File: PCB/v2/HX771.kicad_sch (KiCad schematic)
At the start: 15 parts

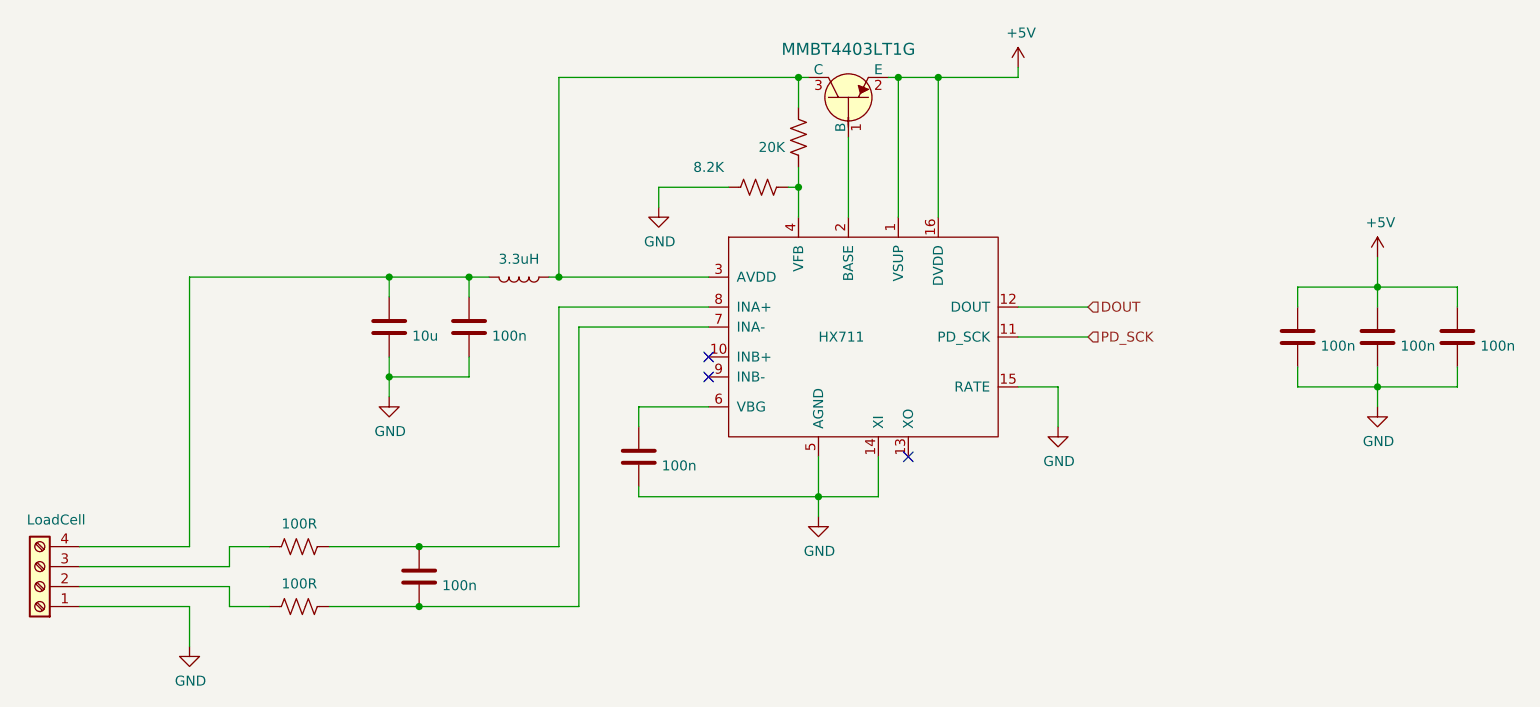
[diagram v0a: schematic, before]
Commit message: WIP updated symbols for tmc5106
Updated footprint for tmc5106,
need to check how motor wiring is done, might be wired up stupid before and that's gonna be sad
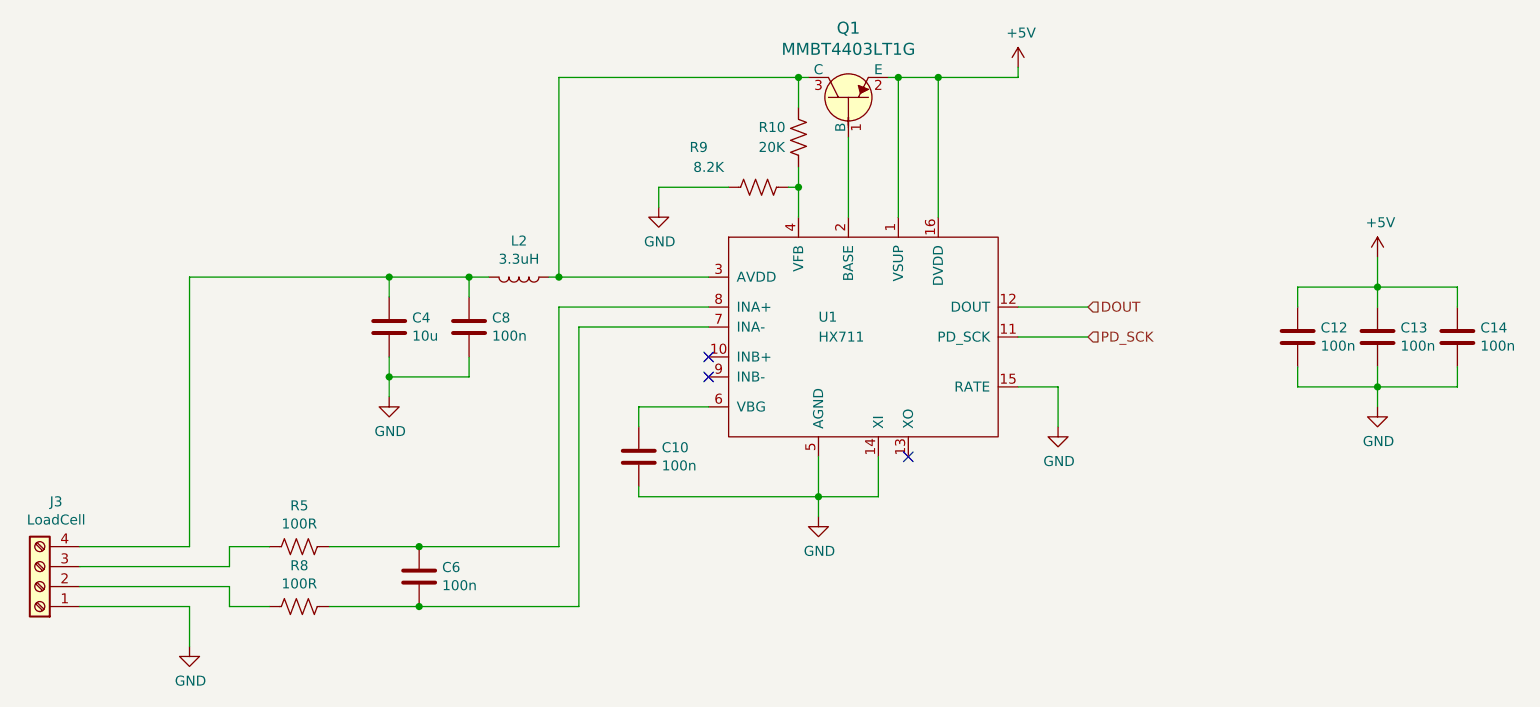
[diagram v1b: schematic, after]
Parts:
- gave numbers to parts that had none: 15
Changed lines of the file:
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@@
   (symbol (lib_id "MMTK:HX711") (at 127 85.09 0) (unit 1)
     (in_bom yes) (on_board yes)
-    (property "Reference" "" (id 0) (at 138.43 95.25 0)
+    (property "Reference" "U1" (id 0) (at 138.43 95.25 0)
       (effects (font (size 1.27 1.27)) (justify left))
     )
@@
   (symbol (lib_id "MMTK-rescue:R_US-Device-MMTK-rescue-MMTK-rescue") (at 135.89 72.39 180) (unit 1)
     (in_bom yes) (on_board yes)
-    (property "Reference" "" (id 0) (at 130.81 71.12 0)
+    (property "Reference" "R10" (id 0) (at 130.81 71.12 0)
       (effects (font (size 1.27 1.27)) (justify right))
     )
@@
   (symbol (lib_id "MMTK-rescue:R_US-Device-MMTK-rescue-MMTK-rescue") (at 130.81 78.74 90) (unit 1)
     (in_bom yes) (on_board yes)
-    (property "Reference" "" (id 0) (at 123.19 73.66 90))
+    (property "Reference" "R9" (id 0) (at 123.19 73.66 90))
     (property "Value" "8.2K" (id 1) (at 124.46 76.2 90))
     (property "Footprint" "Resistor_SMD:R_0603_1608Metric" (id 2) (at 131.064 77.724 90)
@@
   (symbol (lib_id "MMTK-rescue:GND-power-MMTK-rescue-MMTK-rescue") (at 118.11 81.28 0) (unit 1)
     (in_bom yes) (on_board yes)
-    (property "Reference" "" (id 0) (at 118.11 87.63 0)
+    (property "Reference" "#PWR0113" (id 0) (at 118.11 87.63 0)
       (effects (font (size 1.27 1.27)) hide)
     )
@@
   (symbol (lib_id "MMTK-rescue:C-Device-MMTK-rescue-MMTK-rescue") (at 115.57 113.03 0) (unit 1)
     (in_bom yes) (on_board yes)
-    (property "Reference" "" (id 0) (at 118.491 111.8616 0)
+    (property "Reference" "C10" (id 0) (at 118.491 111.8616 0)
       (effects (font (size 1.27 1.27)) (justify left))
     )
@@
   (symbol (lib_id "MMTK-rescue:GND-power-MMTK-rescue-MMTK-rescue") (at 138.43 120.65 0) (unit 1)
     (in_bom yes) (on_board yes)
-    (property "Reference" "" (id 0) (at 138.43 127 0)
+    (property "Reference" "#PWR0114" (id 0) (at 138.43 127 0)
       (effects (font (size 1.27 1.27)) hide)
     )
@@
   (symbol (lib_id "MMTK-rescue:GND-power-MMTK-rescue-MMTK-rescue") (at 168.91 109.22 0) (unit 1)
     (in_bom yes) (on_board yes)
-    (property "Reference" "" (id 0) (at 168.91 115.57 0)
+    (property "Reference" "#PWR0115" (id 0) (at 168.91 115.57 0)
       (effects (font (size 1.27 1.27)) hide)
     )
@@
   (symbol (lib_id "MMTK-rescue:C-Device-MMTK-rescue-MMTK-rescue") (at 83.82 96.52 0) (unit 1)
     (in_bom yes) (on_board yes)
-    (property "Reference" "" (id 0) (at 86.741 95.3516 0)
+    (property "Reference" "C4" (id 0) (at 86.741 95.3516 0)
       (effects (font (size 1.27 1.27)) (justify left))
     )
@@
   (symbol (lib_id "MMTK-rescue:C-Device-MMTK-rescue-MMTK-rescue") (at 199.39 97.79 0) (unit 1)
     (in_bom yes) (on_board yes)
-    (property "Reference" "" (id 0) (at 202.311 96.6216 0)
+    (property "Reference" "C12" (id 0) (at 202.311 96.6216 0)
       (effects (font (size 1.27 1.27)) (justify left))
     )
@@
   (symbol (lib_id "MMTK-rescue:C-Device-MMTK-rescue-MMTK-rescue") (at 209.55 97.79 0) (unit 1)
     (in_bom yes) (on_board yes)
-    (property "Reference" "" (id 0) (at 212.471 96.6216 0)
+    (property "Reference" "C13" (id 0) (at 212.471 96.6216 0)
       (effects (font (size 1.27 1.27)) (justify left))
     )
@@
   (symbol (lib_id "MMTK-rescue:C-Device-MMTK-rescue-MMTK-rescue") (at 93.98 96.52 0) (unit 1)
     (in_bom yes) (on_board yes)
-    (property "Reference" "" (id 0) (at 96.901 95.3516 0)
+    (property "Reference" "C8" (id 0) (at 96.901 95.3516 0)
       (effects (font (size 1.27 1.27)) (justify left))
     )
@@
   (symbol (lib_id "MMTK-rescue:C-Device-MMTK-rescue-MMTK-rescue") (at 219.71 97.79 0) (unit 1)
     (in_bom yes) (on_board yes)
-    (property "Reference" "" (id 0) (at 222.631 96.6216 0)
+    (property "Reference" "C14" (id 0) (at 222.631 96.6216 0)
       (effects (font (size 1.27 1.27)) (justify left))
     )
@@
   (symbol (lib_id "MMTK-rescue:L-Device-MMTK-rescue-MMTK-rescue") (at 100.33 90.17 270) (unit 1)
     (in_bom yes) (on_board yes)
-    (property "Reference" "" (id 0) (at 100.33 85.5726 90))
+    (property "Reference" "L2" (id 0) (at 100.33 85.5726 90))
     (property "Value" "3.3uH" (id 1) (at 100.33 87.884 90))
     (property "Footprint" "Inductor_SMD:L_0805_2012Metric" (id 2) (at 100.33 90.17 0)
@@
   (symbol (lib_id "MMTK-rescue:GND-power-MMTK-rescue-MMTK-rescue") (at 83.82 105.41 0) (unit 1)
     (in_bom yes) (on_board yes)
-    (property "Reference" "" (id 0) (at 83.82 111.76 0)
+    (property "Reference" "#PWR0116" (id 0) (at 83.82 111.76 0)
       (effects (font (size 1.27 1.27)) hide)
     )
@@
   (symbol (lib_id "MMTK-rescue:GND-power-MMTK-rescue-MMTK-rescue") (at 209.55 106.68 0) (unit 1)
     (in_bom yes) (on_board yes)
-    (property "Reference" "" (id 0) (at 209.55 113.03 0)
+    (property "Reference" "#PWR0117" (id 0) (at 209.55 113.03 0)
       (effects (font (size 1.27 1.27)) hide)
     )
@@
   (symbol (lib_id "MMTK-rescue:+5V-power-MMTK-rescue-MMTK-rescue") (at 163.83 63.5 0) (unit 1)
     (in_bom yes) (on_board yes)
-    (property "Reference" "" (id 0) (at 163.83 67.31 0)
+    (property "Reference" "#PWR0118" (id 0) (at 163.83 67.31 0)
       (effects (font (size 1.27 1.27)) hide)
     )
@@
   (symbol (lib_id "MMTK-rescue:+5V-power-MMTK-rescue-MMTK-rescue") (at 209.55 87.63 0) (unit 1)
     (in_bom yes) (on_board yes)
-    (property "Reference" "" (id 0) (at 209.55 91.44 0)
+    (property "Reference" "#PWR0119" (id 0) (at 209.55 91.44 0)
       (effects (font (size 1.27 1.27)) hide)
     )
@@
   (symbol (lib_id "MMTK-rescue:C-Device-MMTK-rescue-MMTK-rescue") (at 87.63 128.27 0) (unit 1)
     (in_bom yes) (on_board yes)
-    (property "Reference" "" (id 0) (at 90.551 127.1016 0)
+    (property "Reference" "C6" (id 0) (at 90.551 127.1016 0)
       (effects (font (size 1.27 1.27)) (justify left))
     )
@@
   (symbol (lib_id "MMTK-rescue:R_US-Device-MMTK-rescue-MMTK-rescue") (at 72.39 132.08 270) (unit 1)
     (in_bom yes) (on_board yes)
-    (property "Reference" "" (id 0) (at 72.39 126.873 90))
+    (property "Reference" "R8" (id 0) (at 72.39 126.873 90))
     (property "Value" "100R" (id 1) (at 72.39 129.1844 90))
     (property "Footprint" "Resistor_SMD:R_0603_1608Metric" (id 2) (at 72.136 133.096 90)
@@
   (symbol (lib_id "MMTK-rescue:R_US-Device-MMTK-rescue-MMTK-rescue") (at 72.39 124.46 270) (unit 1)
     (in_bom yes) (on_board yes)
-    (property "Reference" "" (id 0) (at 72.39 119.253 90))
+    (property "Reference" "R5" (id 0) (at 72.39 119.253 90))
     (property "Value" "100R" (id 1) (at 72.39 121.5644 90))
     (property "Footprint" "Resistor_SMD:R_0603_1608Metric" (id 2) (at 72.136 125.476 90)
@@
   (symbol (lib_id "MMTK-rescue:GND-power-MMTK-rescue-MMTK-rescue") (at 58.42 137.16 0) (unit 1)
     (in_bom yes) (on_board yes)
-    (property "Reference" "" (id 0) (at 58.42 143.51 0)
+    (property "Reference" "#PWR0120" (id 0) (at 58.42 143.51 0)
       (effects (font (size 1.27 1.27)) hide)
     )
@@
   (symbol (lib_id "MMTK-rescue:Screw_Terminal_01x04-Connector-MMTK-rescue-MMTK-rescue") (at 39.37 129.54 180) (unit 1)
     (in_bom yes) (on_board yes)
-    (property "Reference" "" (id 0) (at 41.4528 118.745 0))
+    (property "Reference" "J3" (id 0) (at 41.4528 118.745 0))
     (property "Value" "LoadCell" (id 1) (at 41.4528 121.0564 0))
     (property "Footprint" "TerminalBlock_Phoenix:TerminalBlock_Phoenix_PT-1,5-4-3.5-H_1x04_P3.50mm_Horizontal" (id 2) (at 39.37 129.54 0)
@@
   (symbol (lib_id "dk_Transistors-Bipolar-BJT-Single:MMBT4403LT1G") (at 142.24 67.31 270) (mirror x) (unit 1)
     (in_bom yes) (on_board yes)
-    (property "Reference" "" (id 0) (at 142.24 58.4962 90)
+    (property "Reference" "Q1" (id 0) (at 142.24 58.4962 90)
       (effects (font (size 1.524 1.524)))
     )
